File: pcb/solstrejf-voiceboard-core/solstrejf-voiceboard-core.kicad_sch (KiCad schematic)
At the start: 1 part, among them U1 AS3372E

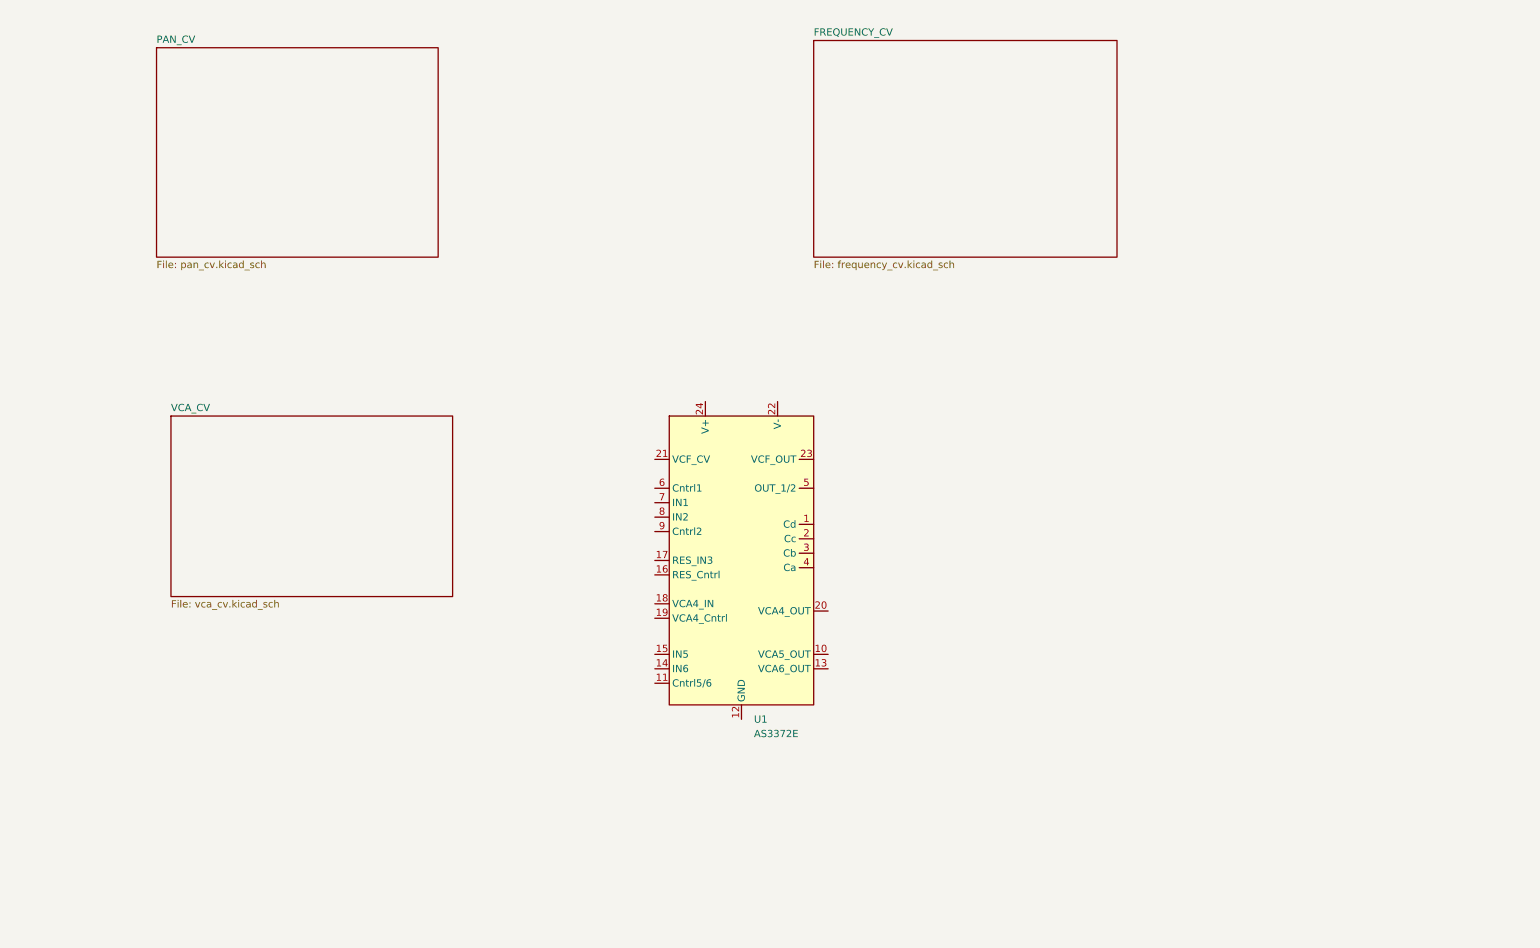
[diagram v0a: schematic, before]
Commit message: Inital draft of the voice board power supplys and core.
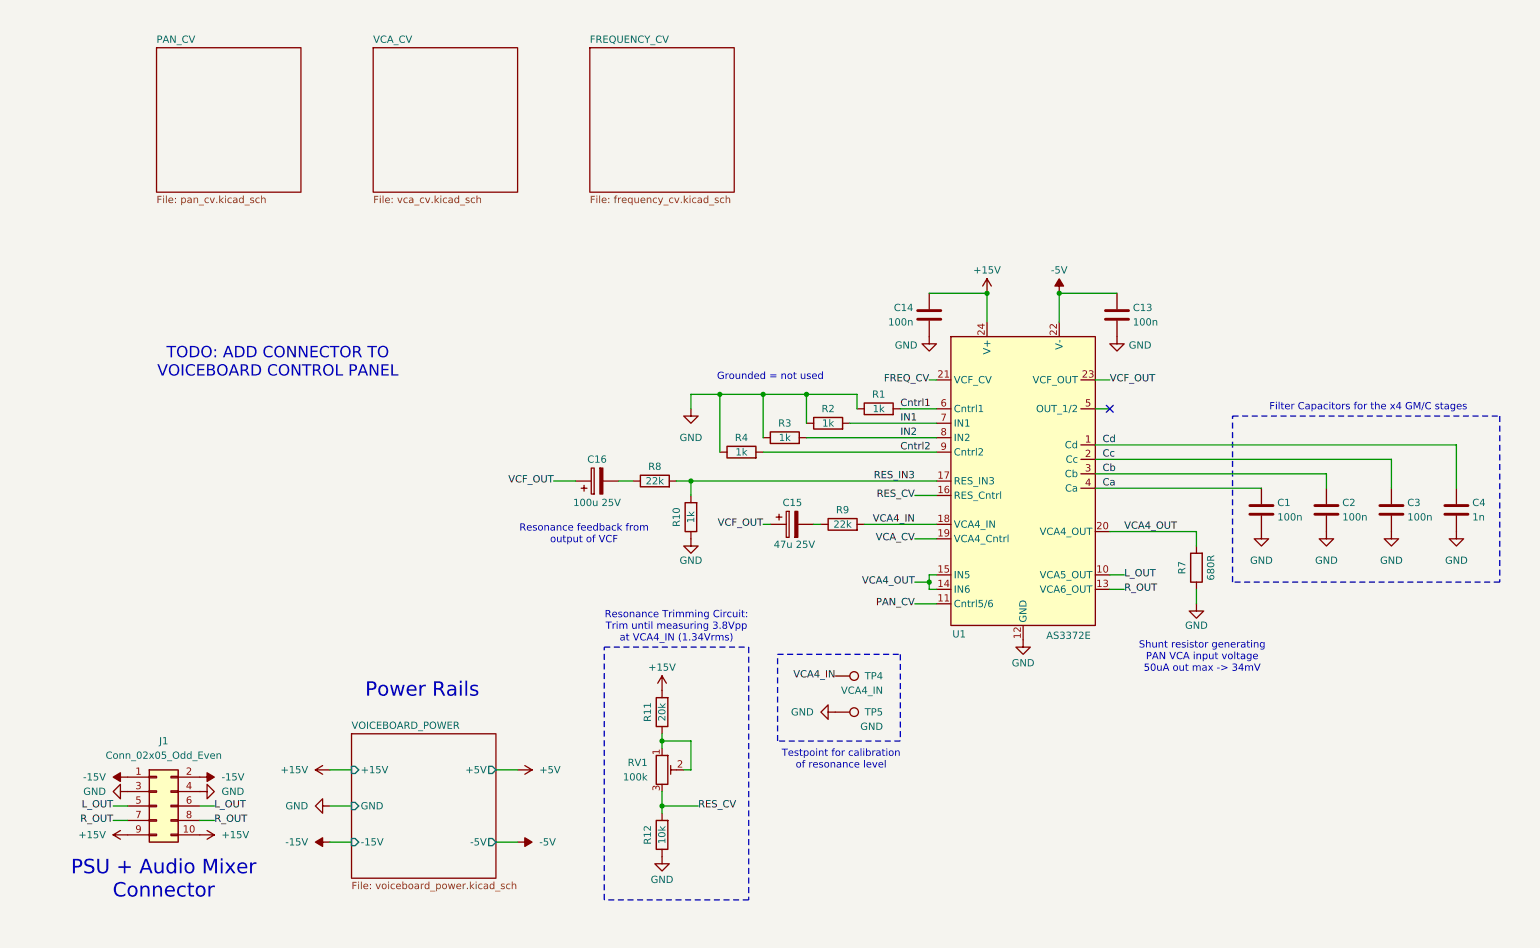
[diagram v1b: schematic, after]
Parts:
- added C1, C13, C14, C2, C3: 100n, Capacitor_THT:C_Disc_D5.0mm_W2.5mm_P5.00mm, symbol Device:C
- added C15: 47u 25V, Capacitor_THT:CP_Radial_D5.0mm_P2.50mm, symbol Device:C_Polarized
- added C16: 100u 25V, Capacitor_THT:CP_Radial_D6.3mm_P2.50mm, symbol Device:C_Polarized
- added C4: 1n, Capacitor_THT:C_Disc_D5.0mm_W2.5mm_P5.00mm, symbol Device:C
- added J1: Conn_02x05_Odd_Even, Connector_IDC:IDC-Header_2x05_P2.54mm_Vertical, symbol Connector_Generic:Conn_02x05_Odd_Even
- added R1, R10, R2, R3, R4: 1k, Resistor_THT:R_Axial_DIN0207_L6.3mm_D2.5mm_P10.16mm_Horizontal, symbol Device:R
- added R11: 20k, Resistor_THT:R_Axial_DIN0207_L6.3mm_D2.5mm_P10.16mm_Horizontal, symbol Device:R
- added R12: 10k, Resistor_THT:R_Axial_DIN0207_L6.3mm_D2.5mm_P10.16mm_Horizontal, symbol Device:R
- added R7: 680R, Resistor_THT:R_Axial_DIN0207_L6.3mm_D2.5mm_P10.16mm_Horizontal, symbol Device:R
- added R8, R9: 22k, Resistor_THT:R_Axial_DIN0207_L6.3mm_D2.5mm_P10.16mm_Horizontal, symbol Device:R
- added RV1: 100k, Potentiometer_THT:Potentiometer_Bourns_3296Y_Vertical, symbol Device:R_Potentiometer_Trim
- added TP4: VCA4_IN, TestPoint:TestPoint_Loop_D2.50mm_Drill1.0mm, symbol Connector:TestPoint
- added TP5: GND, TestPoint:TestPoint_Loop_D2.50mm_Drill1.0mm, symbol Connector:TestPoint
- U1: footprint (none) -> Package_DIP:DIP-24_W7.62mm_Socket
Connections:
- net Cd: now reaches U1.1 (Cd)
- net Cd: now also C4.1
- net L_OUT: now reaches U1.10 (VCA5_OUT)
- net L_OUT: now also J1.5 (Pin_5), J1.6 (Pin_6)
- net PAN_CV: now reaches U1.11 (Cntrl5/6)
- net GND: now reaches U1.12 (GND)
- net GND: now also C1.2, C13.2, C14.2, C2.2, C3.2, C4.2, J1.3 (Pin_3), J1.4 (Pin_4), R1.1, R10.1, R12.1, R2.1, R3.1, R4.1, R7.1, TP5.1
- net R_OUT: now reaches U1.13 (VCA6_OUT)
- net R_OUT: now also J1.7 (Pin_7), J1.8 (Pin_8)
- net VCA4_OUT: now reaches U1.14 (IN6)
- net VCA4_OUT: now also U1.15 (IN5), U1.20 (VCA4_OUT), R7.2
- net RES_CV: now reaches U1.16 (RES_Cntrl)
- net RES_CV: now also R12.2, RV1.3
- net RES_IN3: now reaches U1.17 (RES_IN3)
- net RES_IN3: now also R10.2, R8.2
- net VCA4_IN: now reaches U1.18 (VCA4_IN)
- net VCA4_IN: now also R9.2, TP4.1
- net VCA_CV: now reaches U1.19 (VCA4_Cntrl)
- net Cc: now reaches U1.2 (Cc)
- net Cc: now also C3.1
- net FREQ_CV: now reaches U1.21 (VCF_CV)
- net -5V: now reaches U1.22 (V-)
- net -5V: now also C13.1
- net VCF_OUT: now reaches U1.23 (VCF_OUT)
- net VCF_OUT: now also C15.1, C16.1
- net +15V: now reaches U1.24 (V+)
- net +15V: now also C14.1, J1.10 (Pin_10), J1.9 (Pin_9), R11.2
- net Cb: now reaches U1.3 (Cb)
- net Cb: now also C2.1
- net Ca: now reaches U1.4 (Ca)
- net Ca: now also C1.1
- net Cntrl1: now reaches U1.6 (Cntrl1)
- net Cntrl1: now also R1.2
- net IN1: now reaches U1.7 (IN1)
- net IN1: now also R2.2
- net IN2: now reaches U1.8 (IN2)
- net IN2: now also R3.2
- net Cntrl2: now reaches U1.9 (Cntrl2)
- net Cntrl2: now also R4.2
- new net: R11.1, RV1.1, RV1.2
- new net: C16.2, R8.1
- new net: C15.2, R9.1
- new net -15V: J1.1 (Pin_1), J1.2 (Pin_2)
- no-connect marks 0 -> 1
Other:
- added sheet VOICEBOARD_POWER (voiceboard_power.kicad_sch)
- note added: "Filter Capacitors for the x4 GM/C stages"
- note added: "Grounded = not used"
- note added: "PSU + Audio Mixer Connector"
- note added: "Power Rails"
- note added: "Resonance Trimming Circuit: Trim until measuring 3.8Vpp at VCA4_IN (1.34Vrms)"
- note added: "Resonance feedback from output of VCF"
- note added: "Shunt resistor generating PAN VCA input voltage 50uA out max -> 34mV"
- note added: "TODO: ADD CONNECTOR TO VOICEBOARD CONTROL PANEL"
- note added: "Testpoint for calibration of resonance level"
- title: (none) -> Solstrejf Voiceboard
- moved on the sheet: U1

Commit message: Created hierarchical pins for the three CV sub-circuits and added the rest of the core circuitry for the voice board.
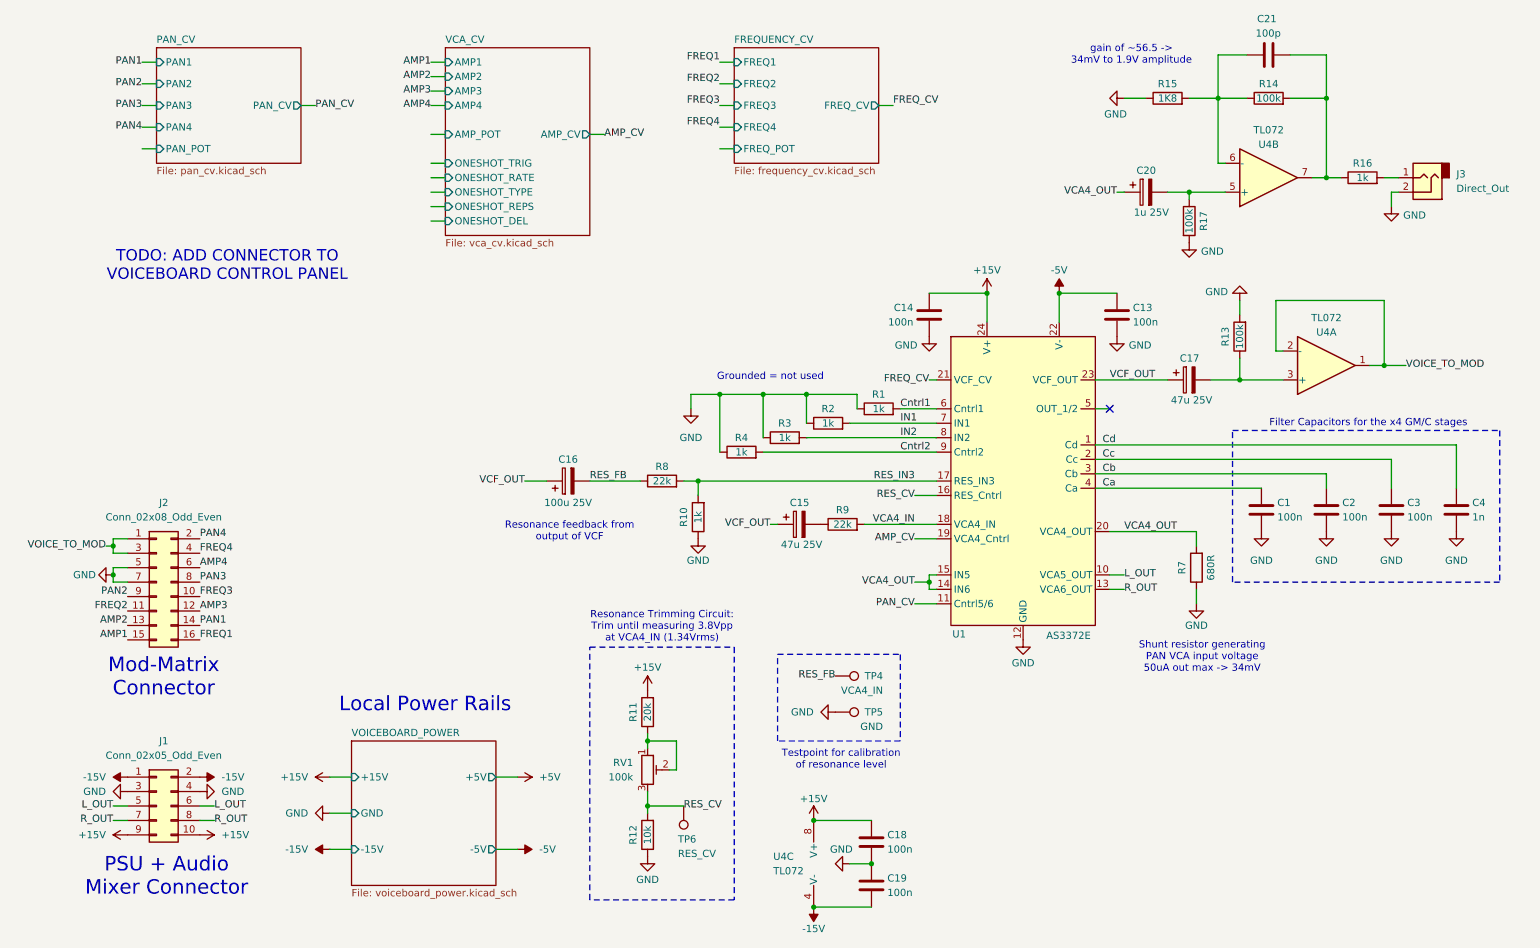
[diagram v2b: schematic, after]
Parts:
- added C17: 47u 25V, Capacitor_THT:CP_Radial_D5.0mm_P2.50mm, symbol Device:C_Polarized
- added C18, C19: 100n, Capacitor_THT:C_Disc_D5.0mm_W2.5mm_P5.00mm, symbol Device:C
- added C20: 1u 25V, Capacitor_THT:CP_Radial_D5.0mm_P2.50mm, symbol Device:C_Polarized
- added C21: 100p, Capacitor_THT:C_Disc_D5.0mm_W2.5mm_P5.00mm, symbol Device:C
- added J2: Conn_02x08_Odd_Even, Connector_IDC:IDC-Header_2x08_P2.54mm_Vertical, symbol Connector_Generic:Conn_02x08_Odd_Even
- added J3: Direct_Out, Connector_PinHeader_2.54mm:PinHeader_1x02_P2.54mm_Vertical, symbol Connector_Audio:AudioJack2
- added R13, R14, R17: 100k, Resistor_THT:R_Axial_DIN0207_L6.3mm_D2.5mm_P10.16mm_Horizontal, symbol Device:R
- added R15: 1K8, Resistor_THT:R_Axial_DIN0207_L6.3mm_D2.5mm_P10.16mm_Horizontal, symbol Device:R
- added R16: 1k, Resistor_THT:R_Axial_DIN0207_L6.3mm_D2.5mm_P10.16mm_Horizontal, symbol Device:R
- added TP6: RES_CV, TestPoint:TestPoint_Loop_D2.50mm_Drill1.0mm, symbol Connector:TestPoint
- added U4: TL072, Package_DIP:DIP-8_W7.62mm_Socket, symbol Amplifier_Operational:TL072
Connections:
- net +15V: now also C18.1, U4.8 (V+)
- net -15V: now also C19.2, U4.4 (V-)
- net GND: now also C18.2, C19.1, J2.5 (Pin_5), J2.7 (Pin_7), J3.2, R13.2, R15.1, R17.2
- net RES_CV: now also TP6.1
- net VCA4_IN: no longer TP4.1
- net VCA4_OUT: now also C20.1
- net VCF_OUT: now also C17.1
- net RES_FB: now reaches C16.2, R8.1
- net RES_FB: now also TP4.1
- net VCA_CV renamed AMP_CV
- new net: C17.2, R13.1, U4.3 (+)
- new net: C21.2, R14.2, R16.1, U4.7
- new net: J3.1, R16.2
- new net: C20.2, R17.1, U4.5 (+)
- new net: C21.1, R14.1, R15.2, U4.6 (-)
- new net AMP1: J2.15 (Pin_15)
- new net AMP2: J2.13 (Pin_13)
- new net AMP3: J2.12 (Pin_12)
- new net AMP4: J2.6 (Pin_6)
- new net FREQ1: J2.16 (Pin_16)
- new net FREQ2: J2.11 (Pin_11)
- new net FREQ3: J2.10 (Pin_10)
- new net FREQ4: J2.4 (Pin_4)
- new net PAN1: J2.14 (Pin_14)
- new net PAN2: J2.9 (Pin_9)
- new net PAN3: J2.8 (Pin_8)
- new net PAN4: J2.2 (Pin_2)
- new net VOICE_TO_MOD: J2.1 (Pin_1), J2.3 (Pin_3), U4.1, U4.2 (-)
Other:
- sheet FREQUENCY_CV ports: added FREQ1, FREQ2, FREQ3, FREQ4, FREQ_CV, FREQ_POT; removed none
- sheet PAN_CV ports: added PAN1, PAN2, PAN3, PAN4, PAN_CV, PAN_POT; removed none
- sheet VCA_CV ports: added AMP1, AMP2, AMP3, AMP4, AMP_CV, AMP_POT, ONESHOT_DEL, ONESHOT_RATE, ONESHOT_REPS, ONESHOT_TRIG, ONESHOT_TYPE; removed none
- note added: "Local Power Rails"
- note added: "Mod-Matrix Connector"
- note added: "gain of ~56.5 -> 34mV to 1.9V amplitude"
- note removed: "Power Rails"
- moved on the sheet: C15, C16, R10, R11, R12, R8, RV1

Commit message: created schematic for CV circuits: PAN, VCA, and FREQ. Created a new symbol for the ONESHOT envelope generator
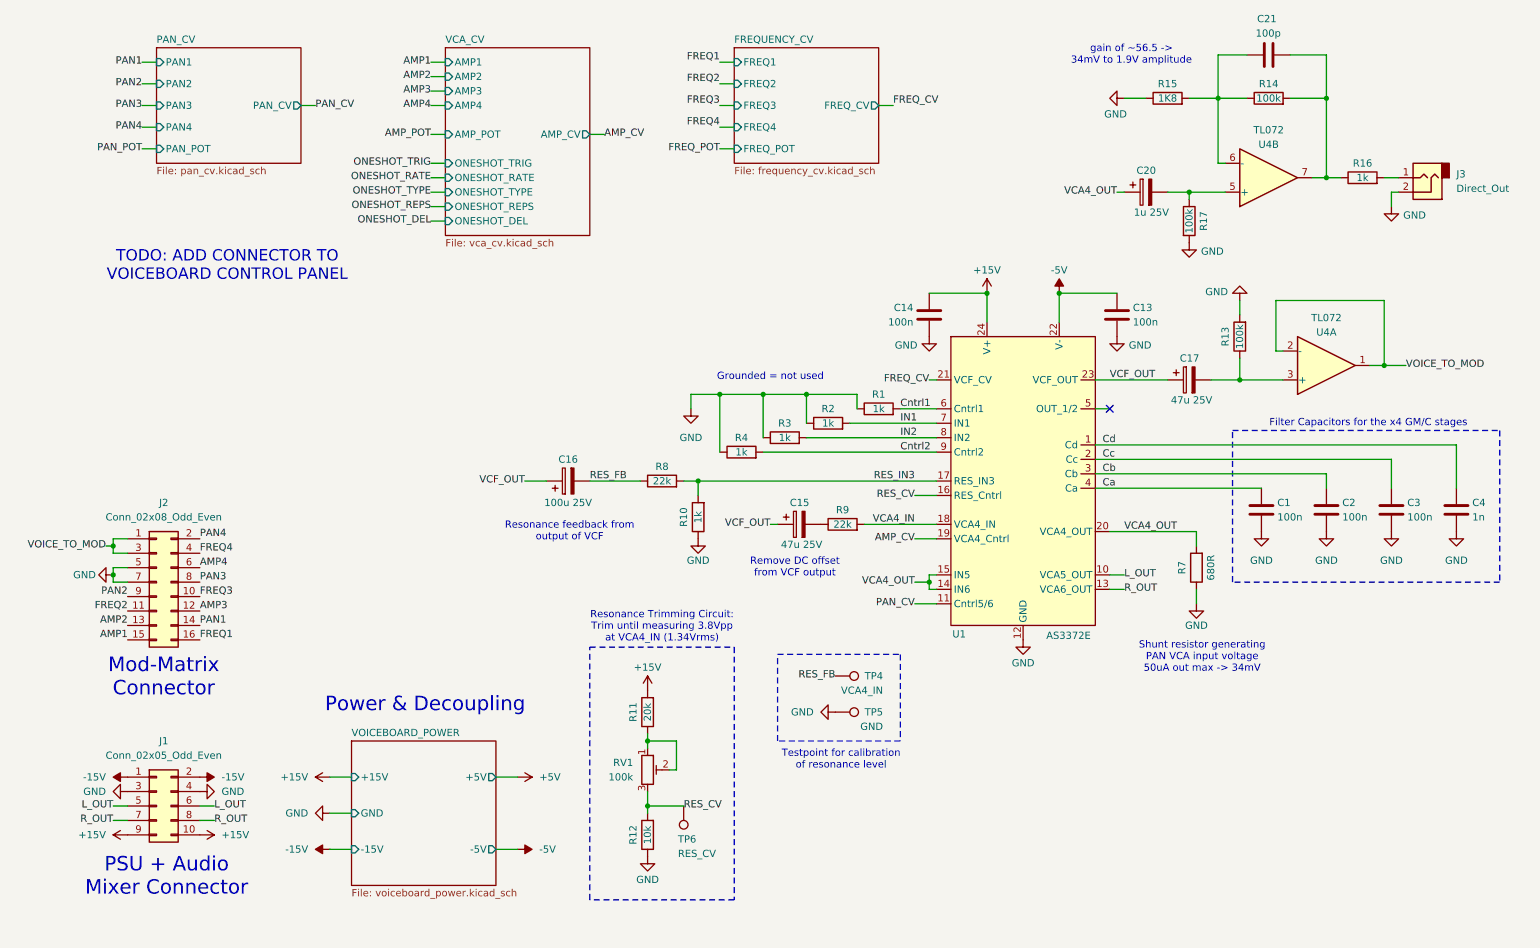
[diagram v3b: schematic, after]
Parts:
- removed C18, C19: 100n, Capacitor_THT:C_Disc_D5.0mm_W2.5mm_P5.00mm, symbol Device:C
- removed unit 3 of U4
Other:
- note added: "Power & Decoupling"
- note added: "Remove DC offset from VCF output"
- note removed: "Local Power Rails"

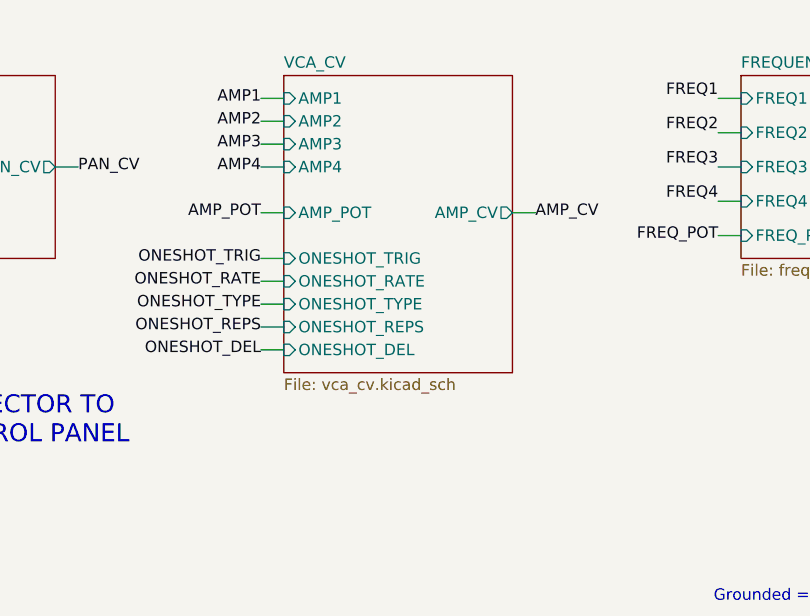
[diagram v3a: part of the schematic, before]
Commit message: updated Kromftronics submodule name and edited path in all PCB projects. Added work-in-progress for the front-panel PCB and the small updates in the voice-board schematic
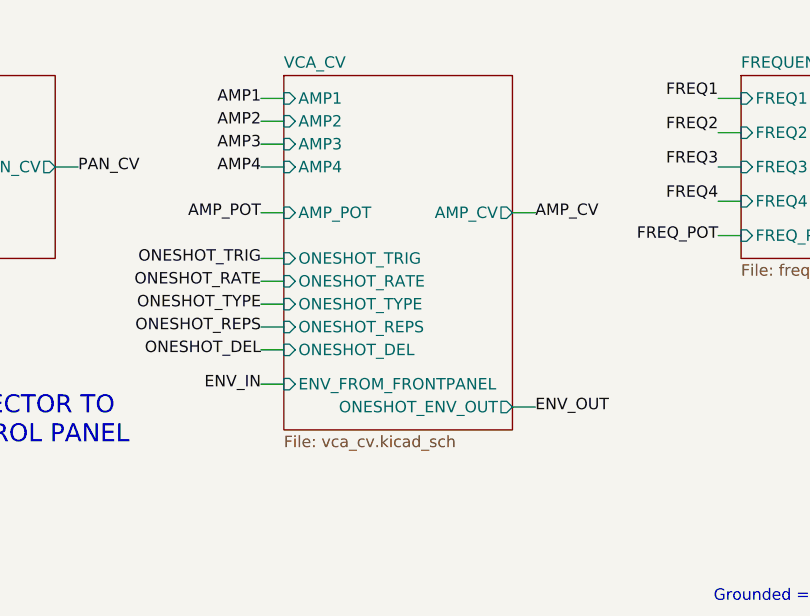
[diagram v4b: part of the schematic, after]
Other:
- sheet VCA_CV ports: added ENV_FROM_FRONTPANEL, ONESHOT_ENV_OUT; removed none
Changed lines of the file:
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@@
 	(wire
 		(pts
+			(xy 86.36 72.39) (xy 88.9 72.39)
+		)
+		(stroke
+			(width 0)
+			(type default)
+		)
+	)
+	(wire
+		(pts
 			(xy 45.72 173.99) (xy 48.26 173.99)
 		)
@@
 	(wire
 		(pts
+			(xy 114.3 74.93) (xy 116.84 74.93)
+		)
+		(stroke
+			(width 0)
+			(type default)
+		)
+	)
+	(wire
+		(pts
 			(xy 30.48 129.54) (xy 30.48 130.81)
 		)
@@
 		)
 	)
+	(label "ENV_IN"
+		(at 86.36 72.39 180)
+		(fields_autoplaced yes)
+		(effects
+			(font
+				(size 1.27 1.27)
+			)
+			(justify right)
+		)
+	)
 	(label "PAN_CV"
 		(at 66.04 48.26 0)
@@
 		)
 	)
+	(label "ENV_OUT"
+		(at 116.84 74.93 0)
+		(fields_autoplaced yes)
+		(effects
+			(font
+				(size 1.27 1.27)
+			)
+			(justify left)
+		)
+	)
 	(label "AMP_CV"
 		(at 171.45 124.46 180)
@@
 	(sheet
 		(at 88.9 38.1)
-		(size 25.4 33.02)
+		(size 25.4 39.37)
 		(fields_autoplaced yes)
 		(stroke
@@
 		)
 		(property "Sheetfile" "vca_cv.kicad_sch"
-			(at 88.9 71.7046 0)
+			(at 88.9 78.0546 0)
 			(effects
 				(font
@@
 			)
 		)
+		(pin "ENV_FROM_FRONTPANEL" input
+			(at 88.9 72.39 180)
+			(effects
+				(font
+					(size 1.27 1.27)
+				)
+				(justify left)
+			)
+		)
+		(pin "ONESHOT_ENV_OUT" output
+			(at 114.3 74.93 0)
+			(effects
+				(font
+					(size 1.27 1.27)
+				)
+				(justify right)
+			)
+		)
